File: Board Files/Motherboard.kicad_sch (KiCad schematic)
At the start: 125 parts, among them P1 72-Pin Connector, P2 EXP-Connector, P3 MOD RF, P4 Controller Input, P5 Controller Input, P6 PWR/RST IN, P8 PWR/RST IN, Q1 2SA937, Q2 2SC2021, Q3 2SC2021, U1 6116 (WRAM), U10 CIC, U2 74HC373, U3 74HC139, U4 6116 (VRAM), U5 RP2C02 PPU, U6 RP2A03 CPU, U7 40H368 (CI), U8 40H368 (CII), U9 74LS04, X1 21.477272 MHz, X2 4MHz

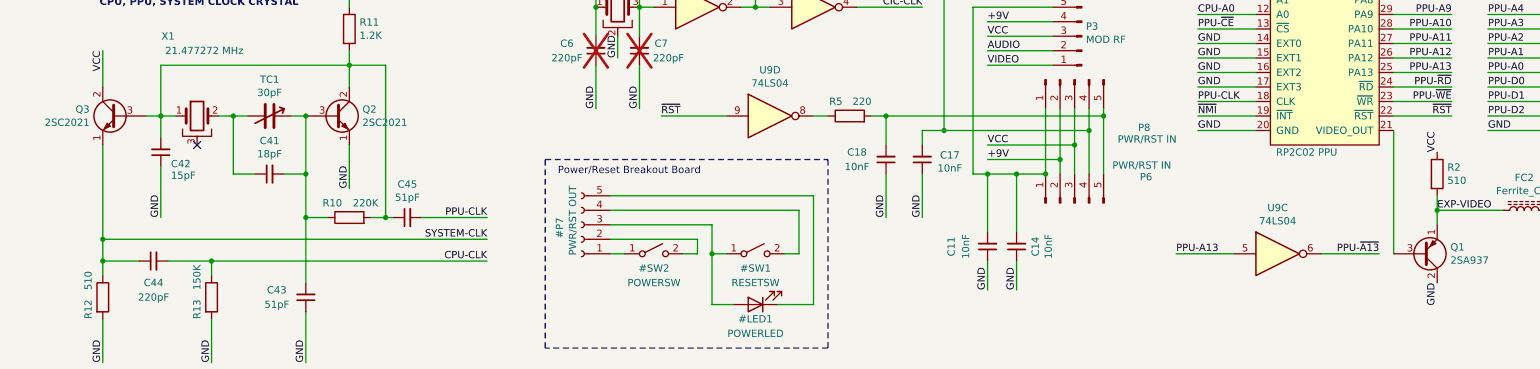
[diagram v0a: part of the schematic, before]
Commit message: feat: updated kicad v9 symbols
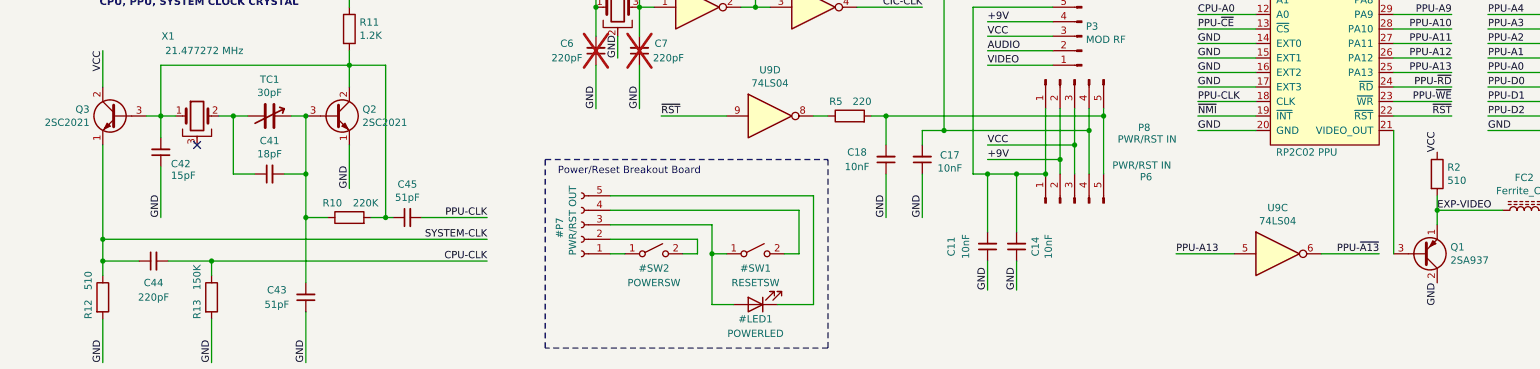
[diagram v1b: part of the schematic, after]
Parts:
- Q1: symbol Device:Q_PNP_ECB -> Transistor_BJT:Q_PNP_ECB
- Q2, Q3: symbol Device:Q_NPN_ECB -> Transistor_BJT:Q_NPN_ECB
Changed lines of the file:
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@@
 	)
 	(symbol
-		(lib_id "Device:Q_PNP_ECB")
+		(lib_id "Transistor_BJT:Q_PNP_ECB")
 		(at 267.97 215.9 0)
 		(mirror x)
@@
 			)
 		)
-		(property "Description" ""
+		(property "Description" "PNP transistor, emitter/collector/base"
 			(at 267.97 215.9 0)
 			(effects
@@
 	)
 	(symbol
-		(lib_id "Device:Q_NPN_ECB")
+		(lib_id "Transistor_BJT:Q_NPN_ECB")
 		(at 77.47 191.77 0)
 		(unit 1)
@@
 			)
 		)
-		(property "Description" ""
+		(property "Description" "NPN transistor, emitter/collector/base"
 			(at 77.47 191.77 0)
 			(effects
@@
 	)
 	(symbol
-		(lib_id "Device:Q_NPN_ECB")
+		(lib_id "Transistor_BJT:Q_NPN_ECB")
 		(at 39.37 191.77 0)
 		(mirror y)
@@
 			)
 		)
-		(property "Description" ""
+		(property "Description" "NPN transistor, emitter/collector/base"
 			(at 39.37 191.77 0)
 			(effects
@@
 			)
 		)
-		(property "Description" ""
+		(property "Description" "Light emitting diode"
 			(at 151.13 224.79 0)
 			(effects
 				(font
+					(size 1.27 1.27)
+				)
+				(hide yes)
+			)
+		)
+		(property "Sim.Pins" "1=K 2=A"
+			(at 151.13 223.012 0)
+			(effects
+				(font

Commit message: fix: 74HC368 bus pin type
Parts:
- U7, U8: footprint Package_DIP:DIP-16_W7.62mm -> Package_DIP:DIP-16_W10.16mm
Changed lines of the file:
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@@
 			)
 		)
-		(property "Footprint" "Package_DIP:DIP-16_W7.62mm"
+		(property "Footprint" "Package_DIP:DIP-16_W10.16mm"
 			(at 189.23 19.05 0)
 			(effects
@@
 			)
 		)
-		(property "Footprint" "Package_DIP:DIP-16_W7.62mm"
+		(property "Footprint" "Package_DIP:DIP-16_W10.16mm"
 			(at 187.96 48.26 0)
 			(effects

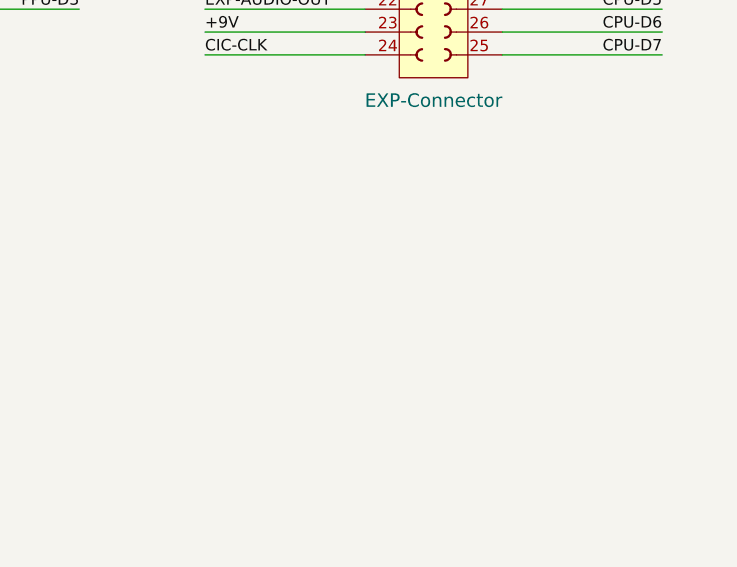
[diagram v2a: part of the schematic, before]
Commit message: feat: added power flag to gnd and vcc nets
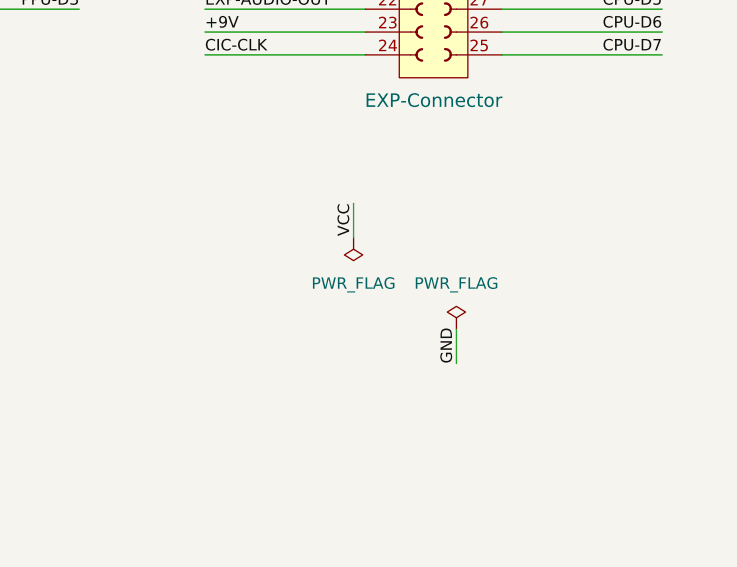
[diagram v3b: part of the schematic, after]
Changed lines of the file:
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@@
 	(wire
 		(pts
+			(xy 353.06 219.71) (xy 353.06 215.9)
+		)
+		(stroke
+			(width 0)
+			(type default)
+		)
+	)
+	(wire
+		(pts
 			(xy 204.47 190.5) (xy 204.47 199.39)
 		)
@@
 	(wire
 		(pts
+			(xy 364.49 229.87) (xy 364.49 233.68)
+		)
+		(stroke
+			(width 0)
+			(type default)
+		)
+	)
+	(wire
+		(pts
 			(xy 171.45 139.7) (xy 181.61 139.7)
 		)
@@
 		)
 	)
+	(label "GND"
+		(at 364.49 233.68 90)
+		(effects
+			(font
+				(size 1.27 1.27)
+			)
+			(justify left bottom)
+		)
+	)
 	(label "CPU-D7"
 		(at 266.7 76.2 180)
@@
 		)
 	)
+	(label "VCC"
+		(at 353.06 215.9 270)
+		(effects
+			(font
+				(size 1.27 1.27)
+			)
+			(justify right bottom)
+		)
+	)
 	(label "GND"
 		(at 130.81 267.97 90)
@@
 	)
 	(symbol
+		(lib_id "power:PWR_FLAG")
+		(at 353.06 219.71 180)
+		(unit 1)
+		(exclude_from_sim no)
+		(in_bom yes)
+		(on_board yes)
+		(dnp no)
+		(fields_autoplaced yes)
+		(property "Reference" "#FLG01"
+			(at 353.06 221.615 0)
+			(effects
+				(font
+					(size 1.27 1.27)
+				)
+				(hide yes)
+			)
+		)
+		(property "Value" "PWR_FLAG"
+			(at 353.06 224.79 0)
+			(effects
+				(font
+					(size 1.27 1.27)
+				)
+			)
+		)
+		(property "Footprint" ""
+			(at 353.06 219.71 0)
+			(effects
+				(font
+					(size 1.27 1.27)
+				)
+				(hide yes)
+			)
+		)
+		(property "Datasheet" "~"
+			(at 353.06 219.71 0)
+			(effects
+				(font
+					(size 1.27 1.27)
+				)
+				(hide yes)
+			)
+		)
+		(property "Description" "Special symbol for telling ERC where power comes from"
+			(at 353.06 219.71 0)
+			(effects
+				(font
+					(size 1.27 1.27)
+				)
+				(hide yes)
+			)
+		)
+		(pin "1"
+		)
+		(instances
+			(project ""
+				(path "/d10b47ec-15d7-4098-8a2a-c0827f933fba"
+					(reference "#FLG01")
+					(unit 1)
+				)
+			)
+		)
+	)
+	(symbol
 		(lib_id "Connector:TestPoint")
 		(at 35.56 143.51 90)
@@
 					(unit 1)
 				)
+			)
+		)
+	)
+	(symbol
+		(lib_id "power:PWR_FLAG")
+		(at 364.49 229.87 0)
+		(unit 1)
+		(exclude_from_sim no)
+		(in_bom yes)
+		(on_board yes)
+		(dnp no)
+		(fields_autoplaced yes)
+		(property "Reference" "#FLG02"
+			(at 364.49 227.965 0)
+			(effects
+				(font
+					(size 1.27 1.27)
+				)
+				(hide yes)
+			)
+		)
+		(property "Value" "PWR_FLAG"
+			(at 364.49 224.79 0)
+			(effects
+				(font
+					(size 1.27 1.27)
+				)
+			)
+		)
+		(property "Footprint" ""
+			(at 364.49 229.87 0)
+			(effects
+				(font
+					(size 1.27 1.27)
+				)
+				(hide yes)
+			)
+		)
+		(property "Datasheet" "~"
+			(at 364.49 229.87 0)
+			(effects
+				(font
+					(size 1.27 1.27)
+				)
+				(hide yes)
+			)
+		)
+		(property "Description" "Special symbol for telling ERC where power comes from"
+			(at 364.49 229.87 0)
+			(effects
+				(font
+					(size 1.27 1.27)
+				)
+				(hide yes)
+			)
+		)
+		(pin "1"
+		)
+		(instances
+			(project ""
+				(path "/d10b47ec-15d7-4098-8a2a-c0827f933fba"
+					(reference "#FLG02")
+					(unit 1)
+				)

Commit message: fix: changed ppu ext pins to passive
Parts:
- U5: footprint Package_DIP:DIP-40_W15.24mm -> Package_DIP:DIP-40_W25.4mm
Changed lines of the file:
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@@
 			)
 		)
-		(property "Footprint" "Package_DIP:DIP-40_W15.24mm"
+		(property "Footprint" "Package_DIP:DIP-40_W25.4mm"
 			(at 251.46 139.7 0)
 			(effects

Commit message: feat: updated footprints to fix DRC errors and warnings
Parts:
- U5: footprint Package_DIP:DIP-40_W25.4mm -> Package_DIP:DIP-40_W15.24mm
- U7, U8: footprint Package_DIP:DIP-16_W10.16mm -> Package_DIP:DIP-16_W7.62mm
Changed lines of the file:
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@@
 			)
 		)
-		(property "Footprint" "Package_DIP:DIP-40_W25.4mm"
+		(property "Footprint" "Package_DIP:DIP-40_W15.24mm"
 			(at 251.46 139.7 0)
 			(effects
@@
 			)
 		)
-		(property "Footprint" "Package_DIP:DIP-16_W10.16mm"
+		(property "Footprint" "Package_DIP:DIP-16_W7.62mm"
 			(at 189.23 19.05 0)
 			(effects
@@
 			)
 		)
-		(property "Footprint" "Package_DIP:DIP-16_W10.16mm"
+		(property "Footprint" "Package_DIP:DIP-16_W7.62mm"
 			(at 187.96 48.26 0)
 			(effects

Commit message: feat: updated trimmer cap footprint
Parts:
- TC1: footprint NESRE:TrimmerCap-THT -> NESRE:Trimmer_Cap_THT_5_5
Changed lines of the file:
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@@
 			)
 		)
-		(property "Footprint" "NESRE:TrimmerCap-THT"
+		(property "Footprint" "NESRE:Trimmer_Cap_THT_5_5"
 			(at 66.04 191.77 0)
 			(effects
